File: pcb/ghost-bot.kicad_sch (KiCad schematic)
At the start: 37 parts, among them J1 Conn_01x03_Pin, J2 Conn_01x03_Pin, J3 Conn_01x04_Pin, J4 Conn_01x02_Pin, J5 Conn_01x05_Pin, J6 Conn_01x04_Pin, SW1 SW_Push, SW2 SW_Push, SW3 Switch

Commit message: Change LED pins (again)
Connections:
- net GND: now also J5.2 (Pin_2); no longer J5.5 (Pin_5)
- net PUSH_BTN1: now also A1.10 (D7); no longer A1.9 (D6)
- net RGB_B: now also A1.9 (D6); no longer A1.10 (D7)
- net RGB_G: now also A1.12 (D9); no longer A1.11 (D8)
- net RGB_R: now also A1.13 (D10); no longer A1.12 (D9)
- net SPI_CLK: now also J5.5 (Pin_5); no longer J5.4 (Pin_4)
- net SPI_MISO: now also A1.15 (D12), J5.1 (Pin_1); no longer A1.13 (D10), J5.3 (Pin_3)
- net SPI_MOSI: now also J5.3 (Pin_3); no longer J5.2 (Pin_2)
- net SPI_SS: now also A1.11 (D8), J5.4 (Pin_4); no longer A1.15 (D12), J5.1 (Pin_1)
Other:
- moved on the sheet: R1, R2, SW1, SW2

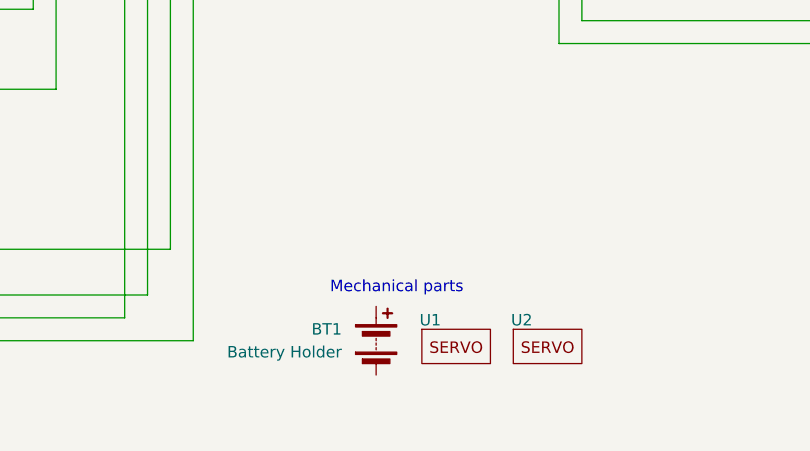
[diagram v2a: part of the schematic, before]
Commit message: Add screws and standoffs to sch to include them in the bom
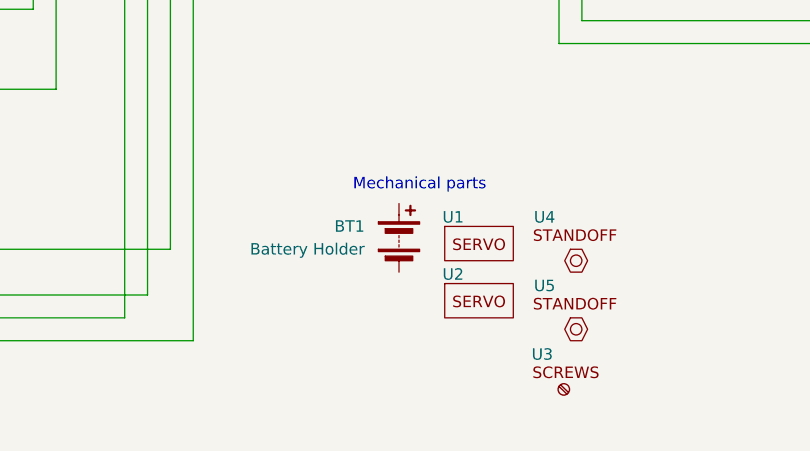
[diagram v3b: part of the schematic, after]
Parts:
- added U3: ~, symbol ghost-bot-symbols:Screws
- added U4, U5: ~, symbol ghost-bot-symbols:Standoff
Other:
- moved on the sheet: BT1, U1, U2

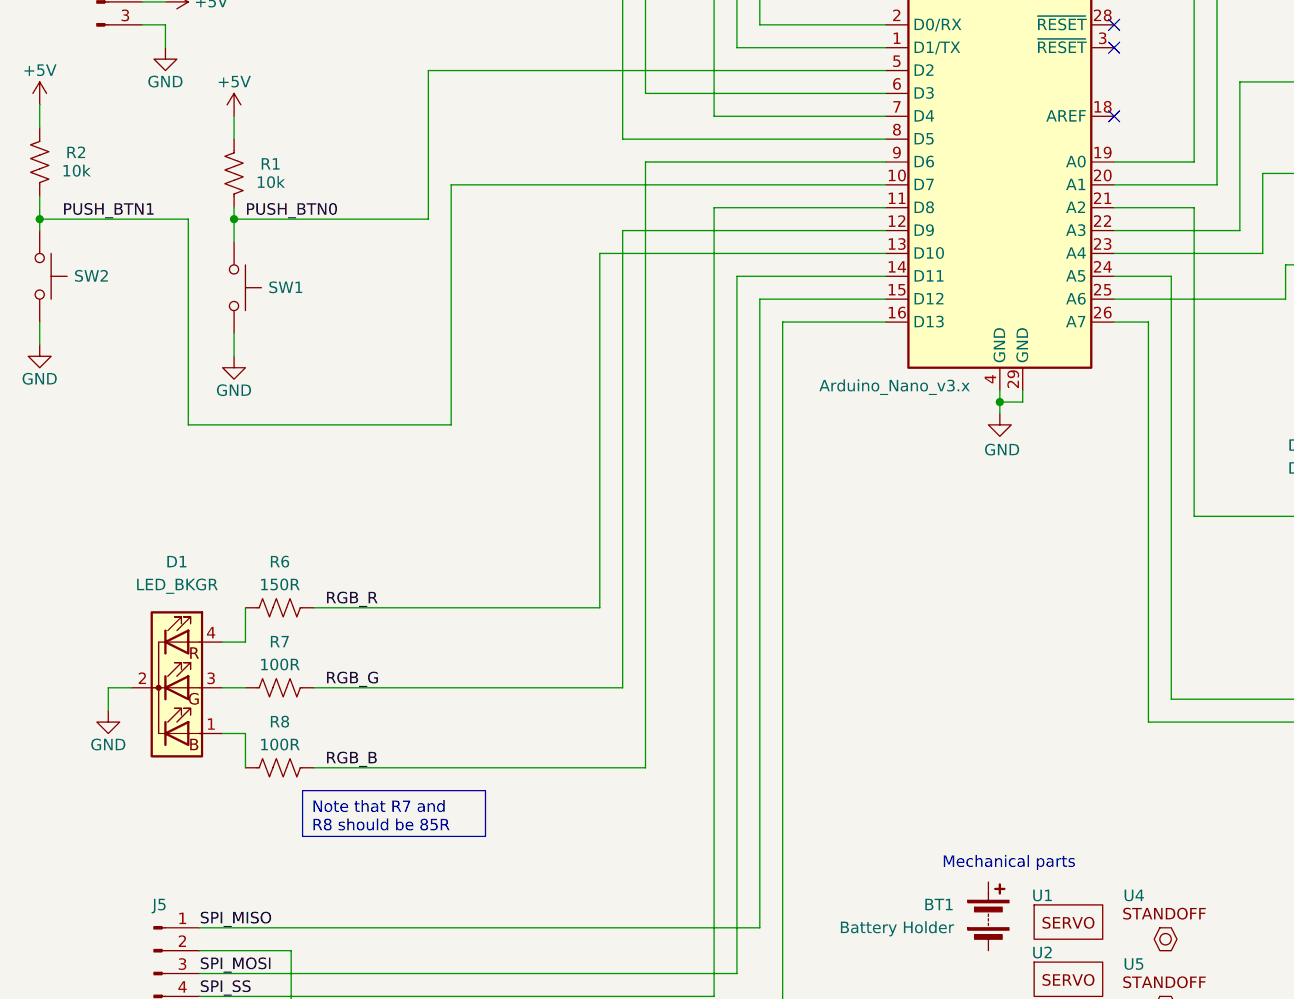
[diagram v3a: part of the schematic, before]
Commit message: Add headers for arduino to plug into so they show up in the bom
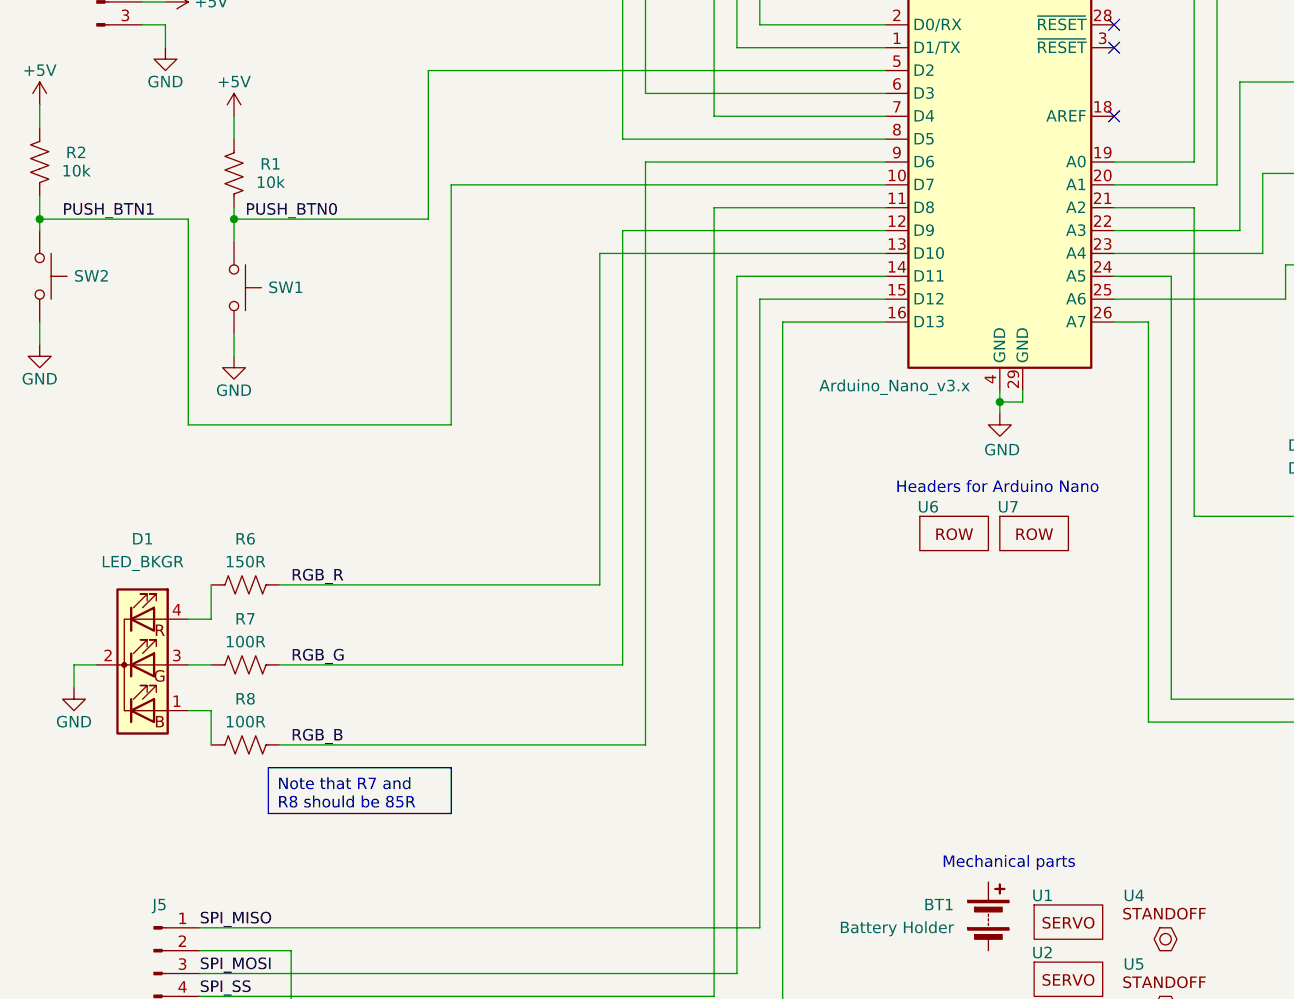
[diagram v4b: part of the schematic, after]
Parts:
- added U6, U7: ~, symbol ghost-bot-symbols:ARDUINO NANO SOCKET ROW
- J5: Manufacturer Part Number (none) -> 2211S-05G; Supplier  (none) -> Element 14; Supplier Part Number (none) -> 1593414
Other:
- note added: "Headers for Arduino Nano"
- moved on the sheet: D1, R6, R7, R8

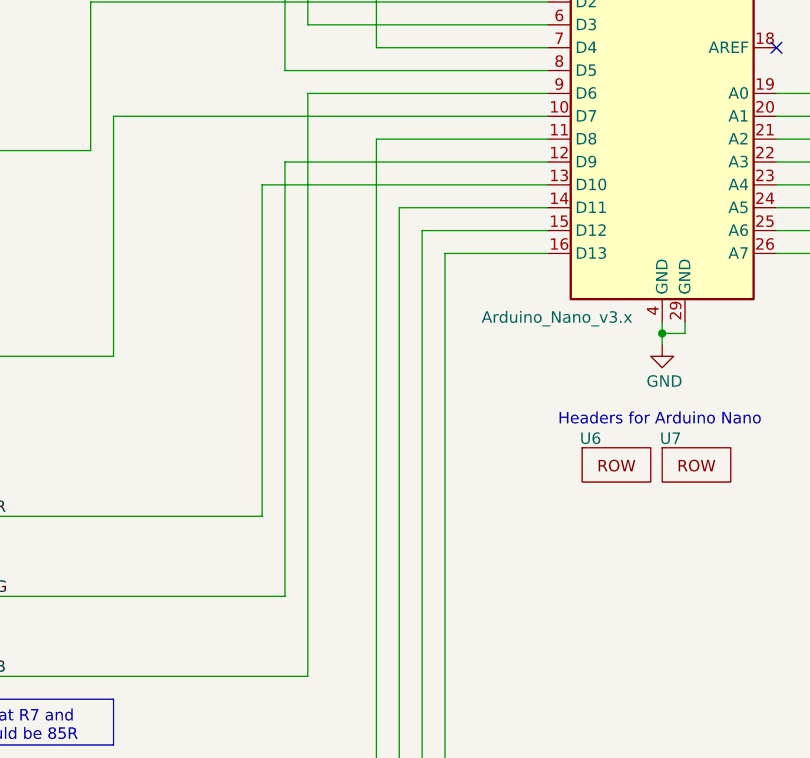
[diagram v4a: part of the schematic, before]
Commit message: Rework traces/placement to work around updated hole positions
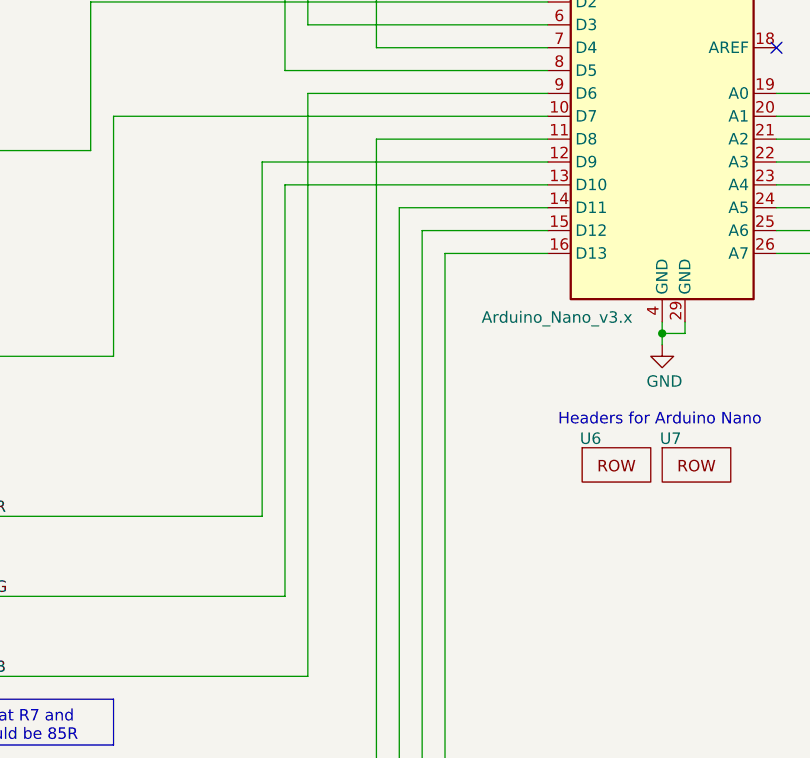
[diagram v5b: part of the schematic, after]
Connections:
- net RGB_G: now also A1.13 (D10); no longer A1.12 (D9)
- net RGB_R: now also A1.12 (D9); no longer A1.13 (D10)
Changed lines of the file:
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@@
 	(title_block
 		(title "Ghost Bot")
-		(date "2024-05-21")
+		(date "2024-05-25")
 		(rev "1.0.0")
 	)
@@
 	(wire
 		(pts
+			(xy 110.49 96.52) (xy 139.7 96.52)
+		)
+		(stroke
+			(width 0)
+			(type default)
+		)
+	)
+	(wire
+		(pts
 			(xy 259.08 115.57) (xy 264.16 115.57)
 		)
@@
 	(wire
 		(pts
-			(xy 139.7 93.98) (xy 110.49 93.98)
-		)
-		(stroke
-			(width 0)
-			(type default)
-		)
-	)
-	(wire
-		(pts
 			(xy 223.52 87.63) (xy 220.98 87.63)
 		)
@@
 	(wire
 		(pts
+			(xy 107.95 93.98) (xy 139.7 93.98)
+		)
+		(stroke
+			(width 0)
+			(type default)
+		)
+	)
+	(wire
+		(pts
 			(xy 62.23 38.1) (xy 62.23 40.64)
 		)
@@
 	(wire
 		(pts
+			(xy 107.95 93.98) (xy 107.95 133.35)
+		)
+		(stroke
+			(width 0)
+			(type default)
+		)
+	)
+	(wire
+		(pts
 			(xy 63.5 179.07) (xy 120.65 179.07)
 		)
@@
 	(wire
 		(pts
-			(xy 107.95 96.52) (xy 107.95 133.35)
-		)
-		(stroke
-			(width 0)
-			(type default)
-		)
-	)
-	(wire
-		(pts
-			(xy 139.7 96.52) (xy 107.95 96.52)
-		)
-		(stroke
-			(width 0)
-			(type default)
-		)
-	)
-	(wire
-		(pts
 			(xy 123.19 30.48) (xy 59.69 30.48)
 		)
@@
 	(wire
 		(pts
-			(xy 176.53 88.9) (xy 165.1 88.9)
+			(xy 110.49 142.24) (xy 110.49 96.52)
 		)
 		(stroke
@@
 	(wire
 		(pts
-			(xy 59.69 38.1) (xy 62.23 38.1)
+			(xy 176.53 88.9) (xy 165.1 88.9)
 		)
 		(stroke
@@
 	(wire
 		(pts
-			(xy 165.1 86.36) (xy 173.99 86.36)
+			(xy 59.69 38.1) (xy 62.23 38.1)
 		)
 		(stroke
@@
 	(wire
 		(pts
-			(xy 165.1 91.44) (xy 173.99 91.44)
+			(xy 165.1 86.36) (xy 173.99 86.36)
 		)
 		(stroke
@@
 	(wire
 		(pts
-			(xy 125.73 101.6) (xy 139.7 101.6)
+			(xy 165.1 91.44) (xy 173.99 91.44)
 		)
 		(stroke
@@
 	(wire
 		(pts
-			(xy 59.69 71.12) (xy 57.15 71.12)
+			(xy 125.73 101.6) (xy 139.7 101.6)
 		)
 		(stroke
@@
 	(wire
 		(pts
-			(xy 110.49 93.98) (xy 110.49 142.24)
+			(xy 59.69 71.12) (xy 57.15 71.12)
 		)
 		(stroke
@@
 		(exclude_from_sim no)
 		(in_bom yes)
-		(on_board yes)
+		(on_board no)
 		(dnp no)
 		(property "Reference" "U7"
@@
 		(exclude_from_sim no)
 		(in_bom yes)
-		(on_board yes)
+		(on_board no)
 		(dnp no)
 		(property "Reference" "U5"
@@
 		(exclude_from_sim no)
 		(in_bom yes)
-		(on_board yes)
+		(on_board no)
 		(dnp no)
 		(property "Reference" "U6"
@@
 		(exclude_from_sim no)
 		(in_bom yes)
-		(on_board yes)
+		(on_board no)
 		(dnp no)
 		(property "Reference" "U4"
@@
 		(exclude_from_sim no)
 		(in_bom yes)
-		(on_board yes)
+		(on_board no)
 		(dnp no)
 		(property "Reference" "U3"

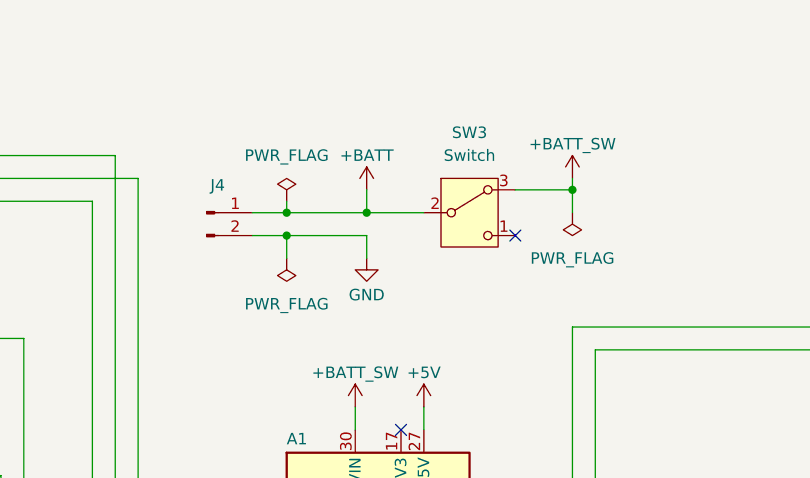
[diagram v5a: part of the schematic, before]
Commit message: Change battery terminal to 2.54mm pitch. Allows "JST" style connector
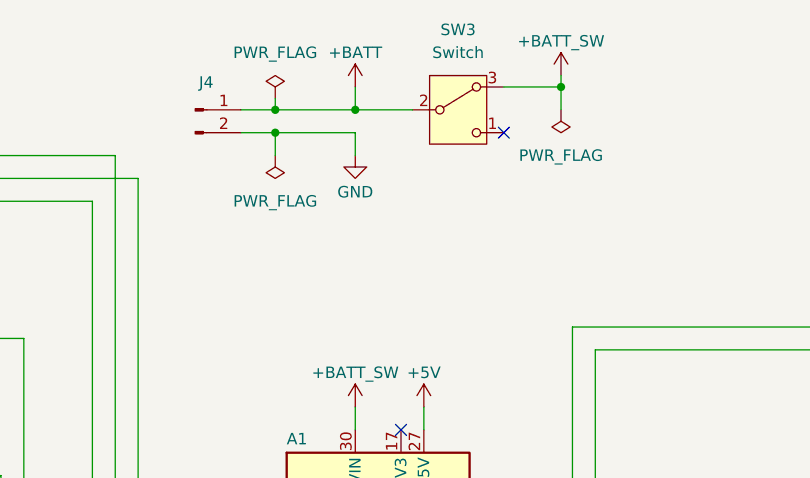
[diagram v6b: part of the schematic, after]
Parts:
- D1: footprint LED_THT:LED_D5.0mm-4_RGB_Staggered_Pins -> ghost-bot-footprints:LED_D5.0mm-4_RGB_Staggered_Pins_fixed-silkscreen
- J4: footprint Connector_Wire:SolderWire-0.1sqmm_1x02_P3.6mm_D0.4mm_OD1mm_Relief -> ghost-bot-footprints:SolderWire-0.1sqmm_1x02_P2.54mm_D0.4mm_OD1mm_Relief
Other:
- moved on the sheet: J4, SW3
